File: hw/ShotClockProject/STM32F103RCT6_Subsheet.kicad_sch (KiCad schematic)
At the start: 41 parts, among them J1 USB4120-03-C_REVA, J2 Conn_ST_STDC14, J3 Conn_01x06_Pin, Q1 Q_NPN_BCE, SW1 SW_SPDT, U1 STM32F103RCT6, U2 LD39015M33R, Y1 16MHz

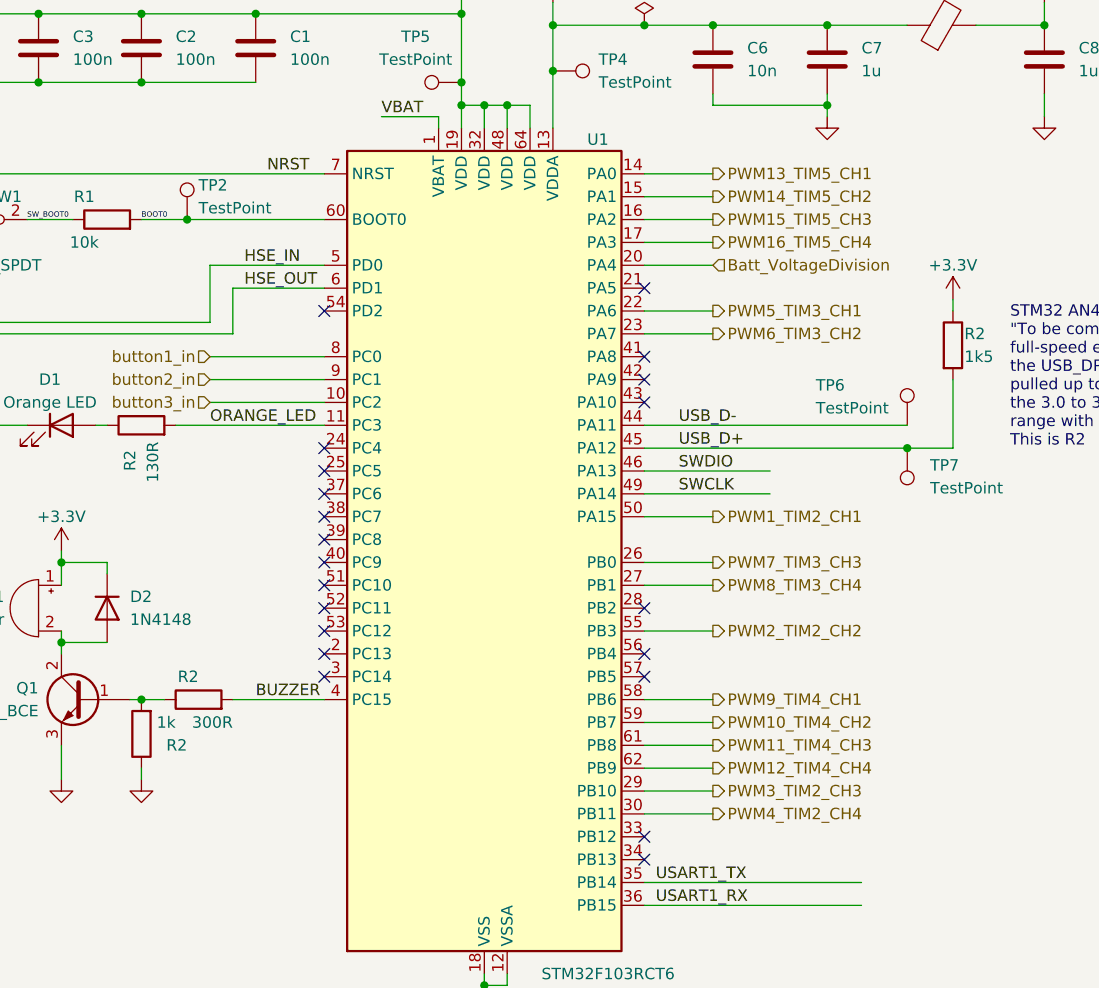
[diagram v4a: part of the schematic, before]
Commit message: Changed pinouts
To only use 1 pwm per display, and GPIo outs for the rest in both HW and firmware
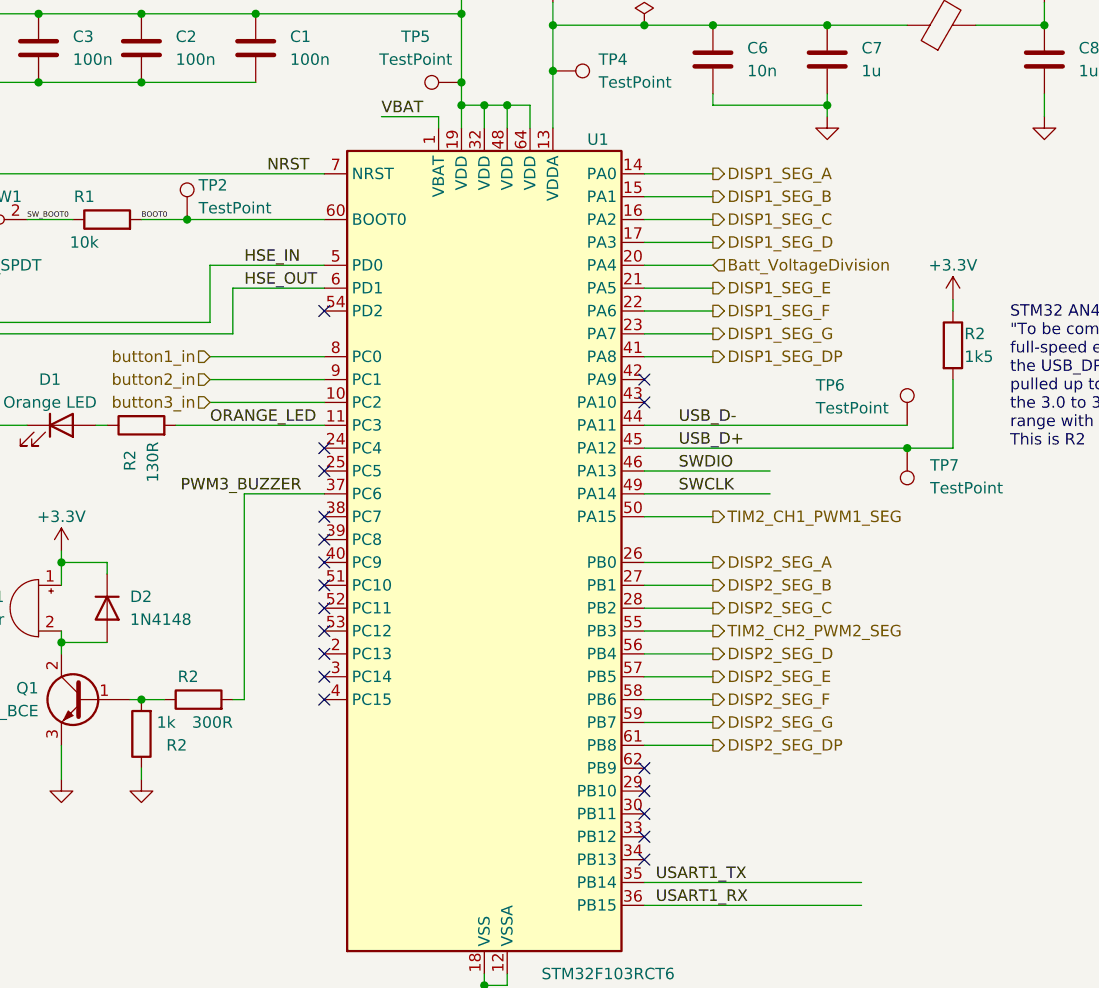
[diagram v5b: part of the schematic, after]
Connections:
- net DISP1_SEG_E: now reaches U1.21 (PA5)
- net DISP2_SEG_C: now reaches U1.28 (PB2)
- net PWM3_BUZZER: now reaches U1.37 (PC6)
- net PWM3_BUZZER: now also R2.2
- net DISP1_SEG_DP: now reaches U1.41 (PA8)
- net DISP2_SEG_D: now reaches U1.56 (PB4)
- net DISP2_SEG_E: now reaches U1.57 (PB5)
- net BUZZER: no longer names the net of U1.4 (PC15)
- net BUZZER: no longer R2.2
- net PWM10_TIM4_CH2 renamed DISP2_SEG_G
- net PWM11_TIM4_CH3 renamed DISP2_SEG_DP
- net PWM12_TIM4_CH4: no longer names the net of U1.62 (PB9)
- net PWM13_TIM5_CH1 renamed DISP1_SEG_A
- net PWM14_TIM5_CH2 renamed DISP1_SEG_B
- net PWM15_TIM5_CH3 renamed DISP1_SEG_C
- net PWM16_TIM5_CH4 renamed DISP1_SEG_D
- net PWM1_TIM2_CH1 renamed TIM2_CH1_PWM1_SEG
- net PWM2_TIM2_CH2 renamed TIM2_CH2_PWM2_SEG
- net PWM3_TIM2_CH3: no longer names the net of U1.29 (PB10)
- net PWM4_TIM2_CH4: no longer names the net of U1.30 (PB11)
- net PWM5_TIM3_CH1 renamed DISP1_SEG_F
- net PWM6_TIM3_CH2 renamed DISP1_SEG_G
- net PWM7_TIM3_CH3 renamed DISP2_SEG_A
- net PWM8_TIM3_CH4 renamed DISP2_SEG_B
- net PWM9_TIM4_CH1 renamed DISP2_SEG_F
- no-connect marks 31 -> 29
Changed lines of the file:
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@@
   (no_connect (at 223.52 59.69))
   (no_connect (at 109.22 110.49))
-  (no_connect (at 144.78 102.87))
   (no_connect (at 109.22 92.71))
   (no_connect (at 259.08 52.07))
-  (no_connect (at 144.78 74.93))
-  (no_connect (at 109.22 90.17))
+  (no_connect (at 144.78 125.73))
   (no_connect (at 224.79 148.59))
   (no_connect (at 252.73 125.73))
@@
   (no_connect (at 144.78 130.81))
   (no_connect (at 144.78 77.47))
-  (no_connect (at 144.78 110.49))
   (no_connect (at 109.22 105.41))
-  (no_connect (at 144.78 67.31))
   (no_connect (at 109.22 85.09))
   (no_connect (at 144.78 80.01))
-  (no_connect (at 144.78 107.95))
   (no_connect (at 144.78 128.27))
   (no_connect (at 252.73 140.97))
@@
   (no_connect (at 109.22 69.85))
   (no_connect (at 109.22 97.79))
+  (no_connect (at 144.78 120.65))
   (no_connect (at 109.22 100.33))
   (no_connect (at 109.22 95.25))
   (no_connect (at 224.79 156.21))
+  (no_connect (at 109.22 113.03))
+  (no_connect (at 144.78 123.19))
   (wire (pts (xy 27.94 92.71) (xy 27.94 96.52))
     (stroke (width 0) (type default))
   )
+  (wire (pts (xy 144.78 102.87) (xy 152.4 102.87))
+    (stroke (width 0) (type default))
+  )
   (wire (pts (xy 39.37 73.66) (xy 34.29 73.66))
     (stroke (width 0) (type default))
@@
     (stroke (width 0) (type default))
   )
+  (wire (pts (xy 144.78 110.49) (xy 152.4 110.49))
+    (stroke (width 0) (type default))
+  )
   (wire (pts (xy 241.3 31.75) (xy 262.89 31.75))
     (stroke (width 0) (type default))
@@
     (stroke (width 0) (type default))
   )
+  (wire (pts (xy 100.33 113.03) (xy 99.06 113.03))
+    (stroke (width 0) (type default))
+  )
   (wire (pts (xy 38.1 125.73) (xy 35.56 125.73))
     (stroke (width 0) (type default))
@@
     (stroke (width 0) (type default))
   )
-  (wire (pts (xy 144.78 123.19) (xy 152.4 123.19))
-    (stroke (width 0) (type default))
-  )
   (wire (pts (xy 27.94 80.01) (xy 27.94 85.09))
     (stroke (width 0) (type default))
@@
     (stroke (width 0) (type default))
   )
-  (wire (pts (xy 144.78 125.73) (xy 152.4 125.73))
-    (stroke (width 0) (type default))
-  )
   (wire (pts (xy 262.89 31.75) (xy 262.89 43.18))
     (stroke (width 0) (type default))
@@
     (stroke (width 0) (type default))
   )
+  (wire (pts (xy 109.22 90.17) (xy 100.33 90.17))
+    (stroke (width 0) (type default))
+  )
   (wire (pts (xy 165.1 45.72) (xy 165.1 46.99))
     (stroke (width 0) (type default))
@@
     (stroke (width 0) (type default))
   )
-  (wire (pts (xy 144.78 120.65) (xy 152.4 120.65))
-    (stroke (width 0) (type default))
-  )
   (wire (pts (xy 127 143.51) (xy 127 144.78))
     (stroke (width 0) (type default))
   )
-  (wire (pts (xy 99.06 113.03) (xy 109.22 113.03))
-    (stroke (width 0) (type default))
-  )
   (wire (pts (xy 30.48 123.19) (xy 35.56 123.19))
     (stroke (width 0) (type default))
@@
     (stroke (width 0) (type default))
   )
+  (wire (pts (xy 144.78 74.93) (xy 152.4 74.93))
+    (stroke (width 0) (type default))
+  )
   (wire (pts (xy 124.46 44.45) (xy 124.46 46.99))
     (stroke (width 0) (type default))
@@
   )
   (wire (pts (xy 88.9 120.65) (xy 88.9 121.92))
+    (stroke (width 0) (type default))
+  )
+  (wire (pts (xy 100.33 90.17) (xy 100.33 113.03))
+    (stroke (width 0) (type default))
+  )
+  (wire (pts (xy 144.78 107.95) (xy 152.4 107.95))
+    (stroke (width 0) (type default))
+  )
+  (wire (pts (xy 144.78 67.31) (xy 152.4 67.31))
     (stroke (width 0) (type default))
   )
@@
     (effects (font (size 1.27 1.27)) (justify left bottom))
   )
-  (label "BUZZER" (at 101.6 113.03 0) (fields_autoplaced)
-    (effects (font (size 1.27 1.27)) (justify left bottom))
+  (label "PWM3_BUZZER" (at 106.68 90.17 180) (fields_autoplaced)
+    (effects (font (size 1.27 1.27)) (justify right bottom))
   )
   (label "USART1_RX" (at 195.58 151.13 0) (fields_autoplaced)
@@
     (effects (font (size 1.27 1.27)) (justify left bottom))
   )
-  (hierarchical_label "PWM11_TIM4_CH3" (shape output) (at 152.4 118.11 0) (fields_autoplaced)
+  (hierarchical_label "DISP2_SEG_G" (shape output) (at 152.4 115.57 0) (fields_autoplaced)
+    (effects (font (size 1.27 1.27)) (justify left))
+  )
+  (hierarchical_label "DISP2_SEG_F" (shape output) (at 152.4 113.03 0) (fields_autoplaced)
     (effects (font (size 1.27 1.27)) (justify left))
   )
@@
     (effects (font (size 1.27 1.27)) (justify right))
   )
-  (hierarchical_label "PWM8_TIM3_CH4" (shape output) (at 152.4 100.33 0) (fields_autoplaced)
-    (effects (font (size 1.27 1.27)) (justify left))
-  )
-  (hierarchical_label "PWM3_TIM2_CH3" (shape output) (at 152.4 123.19 0) (fields_autoplaced)
-    (effects (font (size 1.27 1.27)) (justify left))
-  )
-  (hierarchical_label "PWM1_TIM2_CH1" (shape output) (at 152.4 92.71 0) (fields_autoplaced)
-    (effects (font (size 1.27 1.27)) (justify left))
-  )
-  (hierarchical_label "PWM15_TIM5_CH3" (shape output) (at 152.4 59.69 0) (fields_autoplaced)
-    (effects (font (size 1.27 1.27)) (justify left))
-  )
-  (hierarchical_label "PWM4_TIM2_CH4" (shape output) (at 152.4 125.73 0) (fields_autoplaced)
-    (effects (font (size 1.27 1.27)) (justify left))
-  )
-  (hierarchical_label "PWM14_TIM5_CH2" (shape output) (at 152.4 57.15 0) (fields_autoplaced)
+  (hierarchical_label "DISP2_SEG_E" (shape output) (at 152.4 110.49 0) (fields_autoplaced)
+    (effects (font (size 1.27 1.27)) (justify left))
+  )
+  (hierarchical_label "DISP1_SEG_A" (shape output) (at 152.4 54.61 0) (fields_autoplaced)
+    (effects (font (size 1.27 1.27)) (justify left))
+  )
+  (hierarchical_label "TIM2_CH1_PWM1_SEG" (shape output) (at 152.4 92.71 0) (fields_autoplaced)
+    (effects (font (size 1.27 1.27)) (justify left))
+  )
+  (hierarchical_label "DISP1_SEG_DP" (shape output) (at 152.4 74.93 0) (fields_autoplaced)
+    (effects (font (size 1.27 1.27)) (justify left))
+  )
+  (hierarchical_label "DISP2_SEG_C" (shape output) (at 152.4 102.87 0) (fields_autoplaced)
+    (effects (font (size 1.27 1.27)) (justify left))
+  )
+  (hierarchical_label "DISP2_SEG_B" (shape output) (at 152.4 100.33 0) (fields_autoplaced)
     (effects (font (size 1.27 1.27)) (justify left))
   )
@@
     (effects (font (size 1.27 1.27)) (justify right))
   )
+  (hierarchical_label "DISP2_SEG_DP" (shape output) (at 152.4 118.11 0) (fields_autoplaced)
+    (effects (font (size 1.27 1.27)) (justify left))
+  )
   (hierarchical_label "button2_in" (shape input) (at 96.52 77.47 180) (fields_autoplaced)
     (effects (font (size 1.27 1.27)) (justify right))
   )
-  (hierarchical_label "PWM10_TIM4_CH2" (shape output) (at 152.4 115.57 0) (fields_autoplaced)
-    (effects (font (size 1.27 1.27)) (justify left))
-  )
-  (hierarchical_label "PWM9_TIM4_CH1" (shape output) (at 152.4 113.03 0) (fields_autoplaced)
-    (effects (font (size 1.27 1.27)) (justify left))
-  )
-  (hierarchical_label "PWM6_TIM3_CH2" (shape output) (at 152.4 72.39 0) (fields_autoplaced)
-    (effects (font (size 1.27 1.27)) (justify left))
-  )
-  (hierarchical_label "PWM5_TIM3_CH1" (shape output) (at 152.4 69.85 0) (fields_autoplaced)
-    (effects (font (size 1.27 1.27)) (justify left))
-  )
-  (hierarchical_label "PWM13_TIM5_CH1" (shape output) (at 152.4 54.61 0) (fields_autoplaced)
-    (effects (font (size 1.27 1.27)) (justify left))
-  )
-  (hierarchical_label "PWM16_TIM5_CH4" (shape output) (at 152.4 62.23 0) (fields_autoplaced)
-    (effects (font (size 1.27 1.27)) (justify left))
-  )
-  (hierarchical_label "PWM7_TIM3_CH3" (shape output) (at 152.4 97.79 0) (fields_autoplaced)
-    (effects (font (size 1.27 1.27)) (justify left))
-  )
-  (hierarchical_label "PWM2_TIM2_CH2" (shape output) (at 152.4 105.41 0) (fields_autoplaced)
+  (hierarchical_label "DISP2_SEG_D" (shape output) (at 152.4 107.95 0) (fields_autoplaced)
+    (effects (font (size 1.27 1.27)) (justify left))
+  )
+  (hierarchical_label "DISP1_SEG_B" (shape output) (at 152.4 57.15 0) (fields_autoplaced)
+    (effects (font (size 1.27 1.27)) (justify left))
+  )
+  (hierarchical_label "DISP1_SEG_C" (shape output) (at 152.4 59.69 0) (fields_autoplaced)
+    (effects (font (size 1.27 1.27)) (justify left))
+  )
+  (hierarchical_label "DISP1_SEG_F" (shape output) (at 152.4 69.85 0) (fields_autoplaced)
+    (effects (font (size 1.27 1.27)) (justify left))
+  )
+  (hierarchical_label "DISP2_SEG_A" (shape output) (at 152.4 97.79 0) (fields_autoplaced)
+    (effects (font (size 1.27 1.27)) (justify left))
+  )
+  (hierarchical_label "DISP1_SEG_G" (shape output) (at 152.4 72.39 0) (fields_autoplaced)
+    (effects (font (size 1.27 1.27)) (justify left))
+  )
+  (hierarchical_label "TIM2_CH2_PWM2_SEG" (shape output) (at 152.4 105.41 0) (fields_autoplaced)
     (effects (font (size 1.27 1.27)) (justify left))
   )
@@
     (effects (font (size 1.27 1.27)) (justify left))
   )
-  (hierarchical_label "PWM12_TIM4_CH4" (shape output) (at 152.4 120.65 0) (fields_autoplaced)
-    (effects (font (size 1.27 1.27)) (justify left))
-  )
+  (hierarchical_label "DISP1_SEG_D" (shape output) (at 152.4 62.23 0) (fields_autoplaced)
+    (effects (font (size 1.27 1.27)) (justify left))
+  )
+  (hierarchical_label "DISP1_SEG_E" (shape output) (at 152.4 67.31 0) (fields_autoplaced)
+    (effects (font (size 1.27 1.27)) (justify left))
+  )
